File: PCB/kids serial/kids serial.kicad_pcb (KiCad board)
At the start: 2 copper layers, 76.2 x 43.2 mm, 6 parts, among them J1 n8 Bus Connector, J2 UARTConnector, J3 PowerViaUSB, U1 6551, X1 CXO_DIP14

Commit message: Last commit for v1
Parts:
- U1: footprint Package_DIP:DIP-28_W15.24mm -> Package_DIP:DIP-28_W15.24mm_Socket

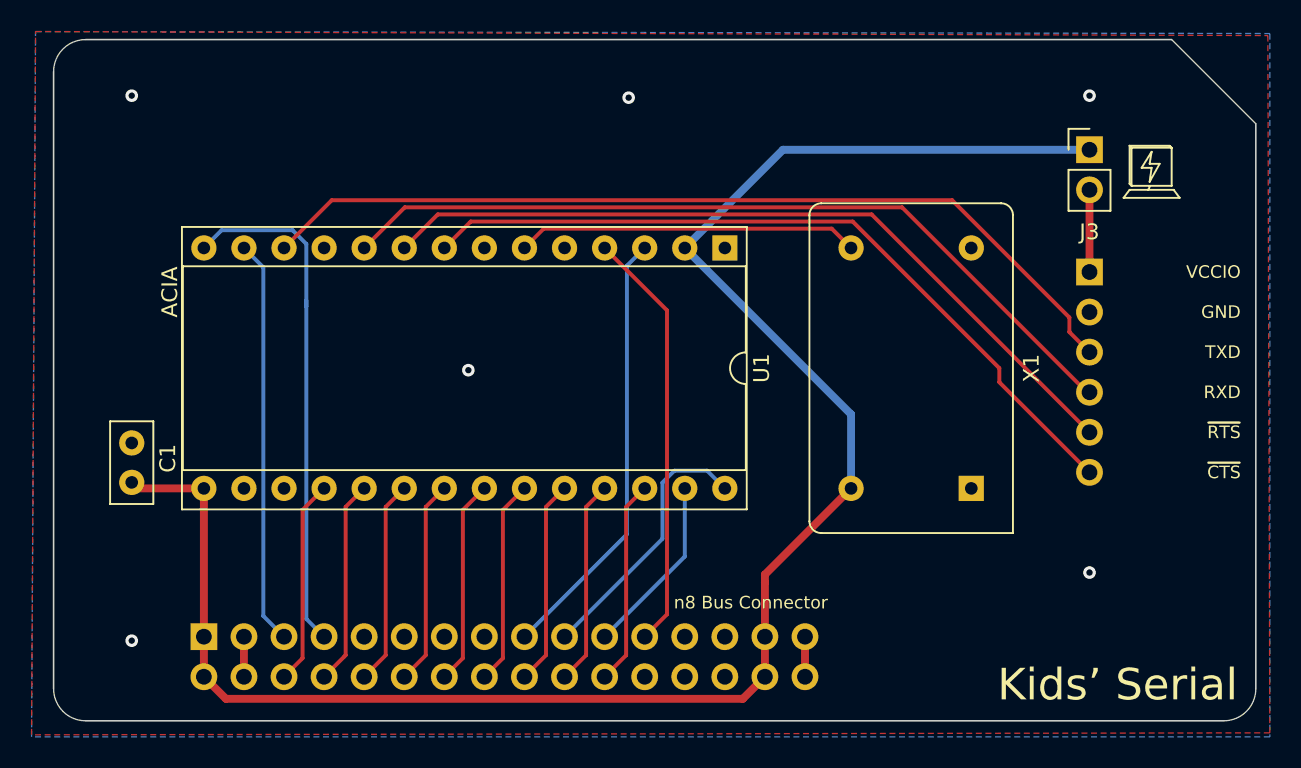
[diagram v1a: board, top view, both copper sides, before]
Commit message: Start of Kids' Serial v2
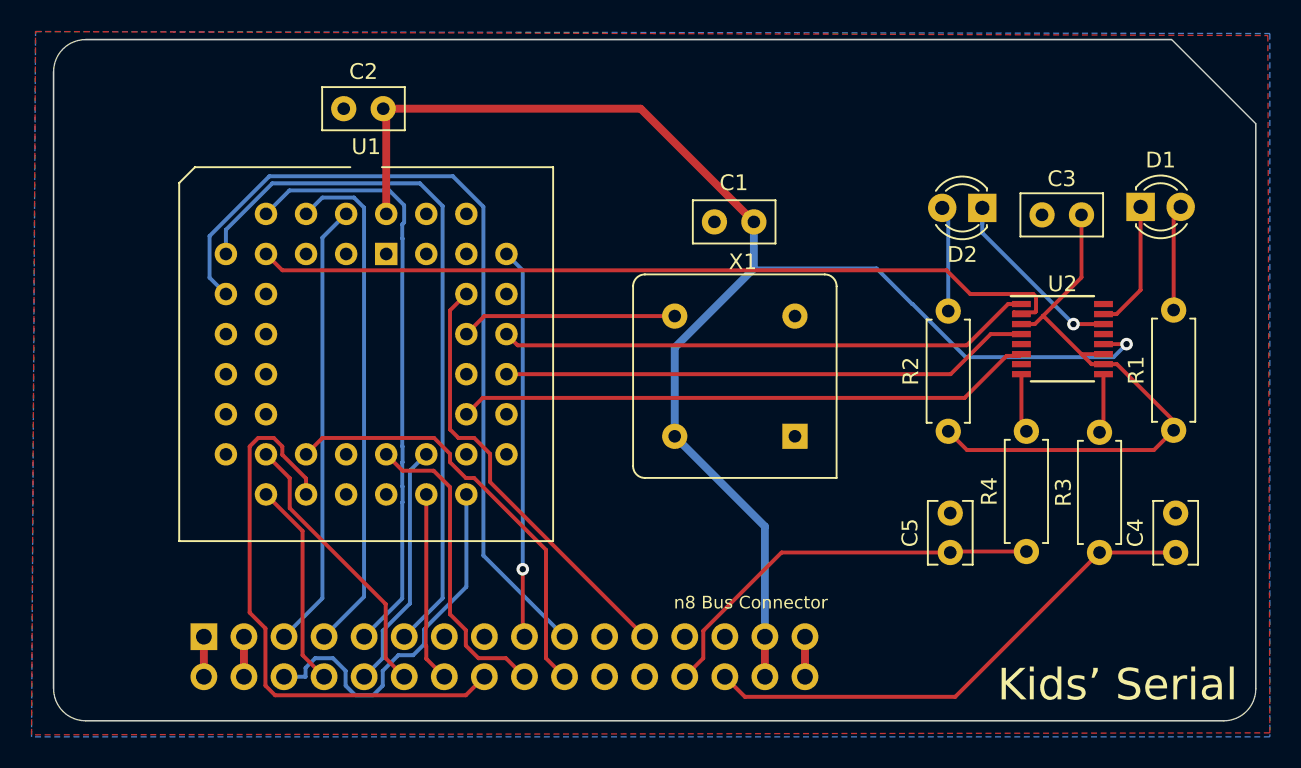
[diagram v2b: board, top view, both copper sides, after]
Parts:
- removed J2: UARTConnector, Connector_PinSocket_2.54mm:PinSocket_1x06_P2.54mm_Horizontal
- removed J3: PowerViaUSB, Connector_PinHeader_2.54mm:PinHeader_1x02_P2.54mm_Vertical
- added C2: 100nF, Capacitor_THT:C_Disc_D5.0mm_W2.5mm_P2.50mm, F.Cu at (121.5, 79.2)
- added C3: 100nF, Capacitor_THT:C_Disc_D5.0mm_W2.5mm_P2.50mm, F.Cu at (165.7, 85.9)
- added C4: 47pF, Capacitor_THT:C_Disc_D3.8mm_W2.6mm_P2.50mm, F.Cu at (171.7, 107.3)
- added C5: 47pF, Capacitor_THT:C_Disc_D3.8mm_W2.6mm_P2.50mm, F.Cu at (157.4, 107.3)
- added D1: TX, LED_THT:LED_D3.0mm, F.Cu at (169.5, 85.4)
- added D2: RX, LED_THT:LED_D3.0mm, F.Cu at (159.4, 85.5)
- added R1: 330, Resistor_THT:R_Axial_DIN0207_L6.3mm_D2.5mm_P7.62mm_Horizontal, F.Cu at (171.6, 99.6)
- added R2: 330, Resistor_THT:R_Axial_DIN0207_L6.3mm_D2.5mm_P7.62mm_Horizontal, F.Cu at (157.3, 99.6)
- added R3: 27, Resistor_THT:R_Axial_DIN0207_L6.3mm_D2.5mm_P7.62mm_Horizontal, F.Cu at (166.9, 99.7)
- added R4: 27, Resistor_THT:R_Axial_DIN0207_L6.3mm_D2.5mm_P7.62mm_Horizontal, F.Cu at (162.2, 99.6)
- added U2: FT230XS, Package_SO:SSOP-16_3.9x4.9mm_P0.635mm, F.Cu at (164.5, 93.8)
- C1: value 100nf -> 100nF
- U1: value 6551 -> SC28L92_PLC44; footprint Package_DIP:DIP-28_W15.24mm_Socket -> Package_LCC:PLCC-44_THT-Socket
- X1: value CXO_DIP14 -> 3.6864Mhz; footprint Oscillator:Oscillator_DIP-14 -> Oscillator:Oscillator_DIP-8
- moved C1 42.8 mm to (145.0, 86.4), turned to 180 degrees
- moved U1 21.5 mm to (121.7, 88.4), turned to 0 degrees
- moved X1 11.7 mm to (147.6, 99.9)
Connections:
- J1 pad 26: Net-(J1-Pad26) -> USB_D+
- J1 pad 28: Net-(J1-Pad28) -> USB_D-
- U1 pad 1: GND -> Net-(U1-Pad1)
- U1 pad 10: RXD_IO -> Net-(U1-Pad10)
- U1 pad 12: TXD_IO -> GND
- U1 pad 13: /A0 -> Net-(U1-Pad13)
- U1 pad 14: /A1 -> Net-(U1-Pad14)
- U1 pad 15: +5V -> Net-(U1-Pad15)
- U1 pad 16: GND -> Net-(U1-Pad16)
- U1 pad 17: GND -> Net-(U1-Pad17)
- U1 pad 18: /D0 -> /D1
- U1 pad 19: /D1 -> /D3
- U1 pad 2: +5V -> /A0
- U1 pad 20: /D2 -> /D5
- U1 pad 21: /D3 -> /D7
- U1 pad 22: /D4 -> GND
- U1 pad 23: /D5 -> Net-(U1-Pad23)
- U1 pad 24: /D6 -> ~IRQ
- U1 pad 25: /D7 -> /D6
- U1 pad 26: ~IRQ -> /D4
- U1 pad 27: CLK -> /D2
- U1 pad 28: R~W -> /D0
- U1 pad 3: ~CS -> Net-(U1-Pad3)
- U1 pad 4: ~RES -> /A1
- U1 pad 6: XTAL_CLK -> /A2
- U1 pad 7: Net-(U1-Pad7) -> /A3
- U1 pad 8: ~CTS_IO -> ~CTS
- U1 pad 9: ~RTS_IO -> R~W
- X1 pad 8: XTAL_CLK -> +5V
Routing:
- net TXD_IO: track 56.8 -> 0.00 mm
- net ~CTS: track 0.00 -> 52.9 mm
- net RXD_IO: track 51.9 -> 0.00 mm
- net ~RTS_IO: track 50.0 -> 0.00 mm
- net ~CTS_IO: track 48.7 -> 0.00 mm
- net /A3: track 0.00 -> 45.4 mm
- net /A2: track 0.00 -> 38.2 mm
- net +3V3: track 0.00 -> 37.3 mm
- net ~RTS: track 0.00 -> 36.8 mm
- net R~W: track 17.1 -> 53.2 mm
- net RxD: track 0.00 -> 34.0 mm
- net TxD: track 0.00 -> 33.7 mm
- net USB_D-: track 0.00 -> 32.9 mm
- net USB_D+: track 0.00 -> 26.0 mm
- net /D5: track 13.0 -> 36.4 mm
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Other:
- board text removed: "ACIA"
- board text removed: "GND"
- board text removed: "RXD"
- board text removed: "TXD"
- board text removed: "VCCIO"
- board text removed: "~CTS"
- board text removed: "~RTS"

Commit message: Nearly final v2 PCBs
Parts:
- moved D1 0.06 mm to (169.5, 85.5)
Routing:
- net GND: track 5.08 -> 40.0 mm, vias 0 -> 10
- net +5V: track 96.8 -> 125.9 mm, vias 1 -> 0
- net ~IRQ: track 0.00 -> 22.1 mm
- net R~W: track 53.2 -> 34.4 mm
- net /D5: track 36.4 -> 19.6 mm
- net /A3: track 45.4 -> 35.5 mm
- net /A0: track 28.4 -> 37.2 mm
- net /D0: track 23.7 -> 17.3 mm
- net /D4: track 12.1 -> 18.0 mm
- net /A2: track 38.2 -> 32.7 mm
- net +3V3: track 37.3 -> 41.1 mm
- net /D2: track 15.7 -> 19.5 mm
- net ~CS: track 24.7 -> 27.0 mm
- net /A1: track 32.6 -> 34.6 mm
- net ~CTS: track 52.9 -> 51.3 mm
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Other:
- net class Default: clearance 0.2 -> 0.16; trace_width 0.25 -> 0.16
- net class Power: clearance 0.3 -> 0.2; trace_width 0.5 -> 0.3
- rule trace_clearance: 0.2 -> 0.16
- rule trace_min: 0.2 -> 0.154
